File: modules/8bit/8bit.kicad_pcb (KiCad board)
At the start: 2 copper layers, 30.5 x 68.6 mm, 24 parts, among them SW1 MODE SELECT, U1 MCP6002-xSN, U2 ATtiny1616-M, U3 MCP6002-xSN

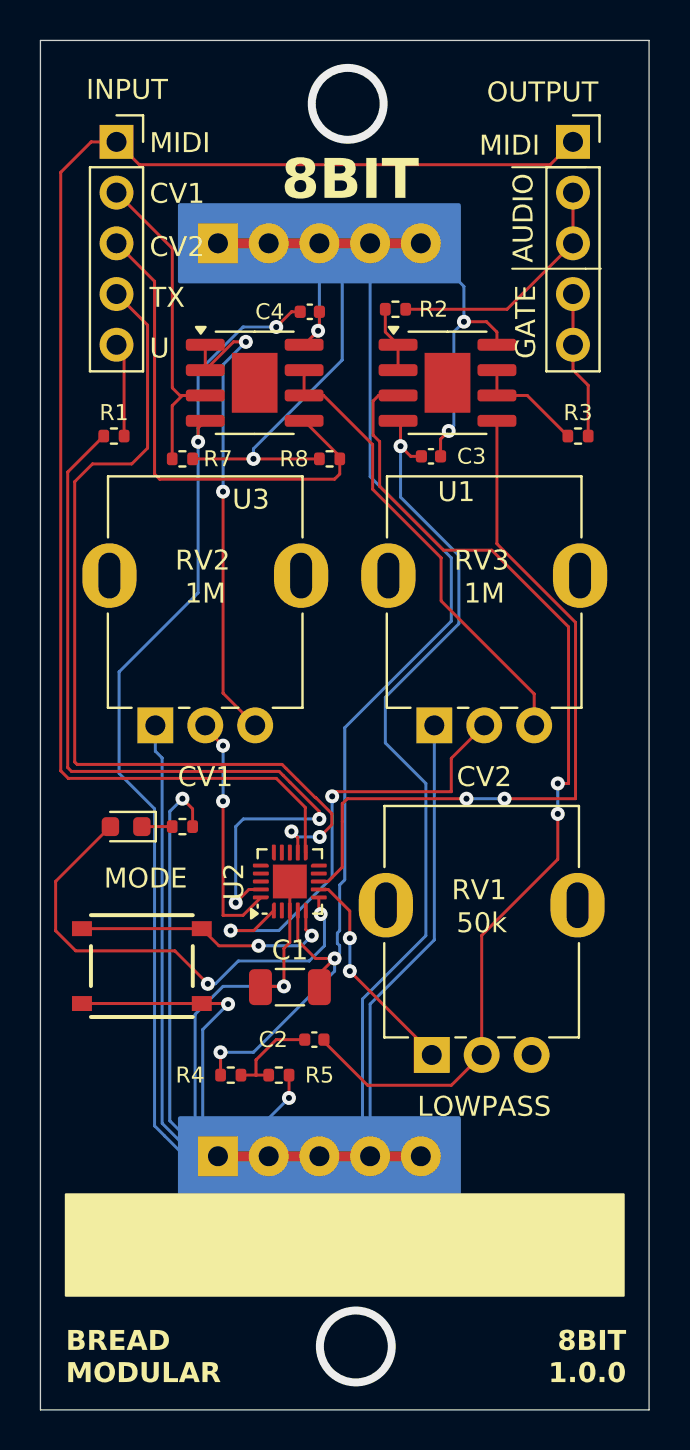
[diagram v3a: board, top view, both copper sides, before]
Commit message: 8bit: Change the push button
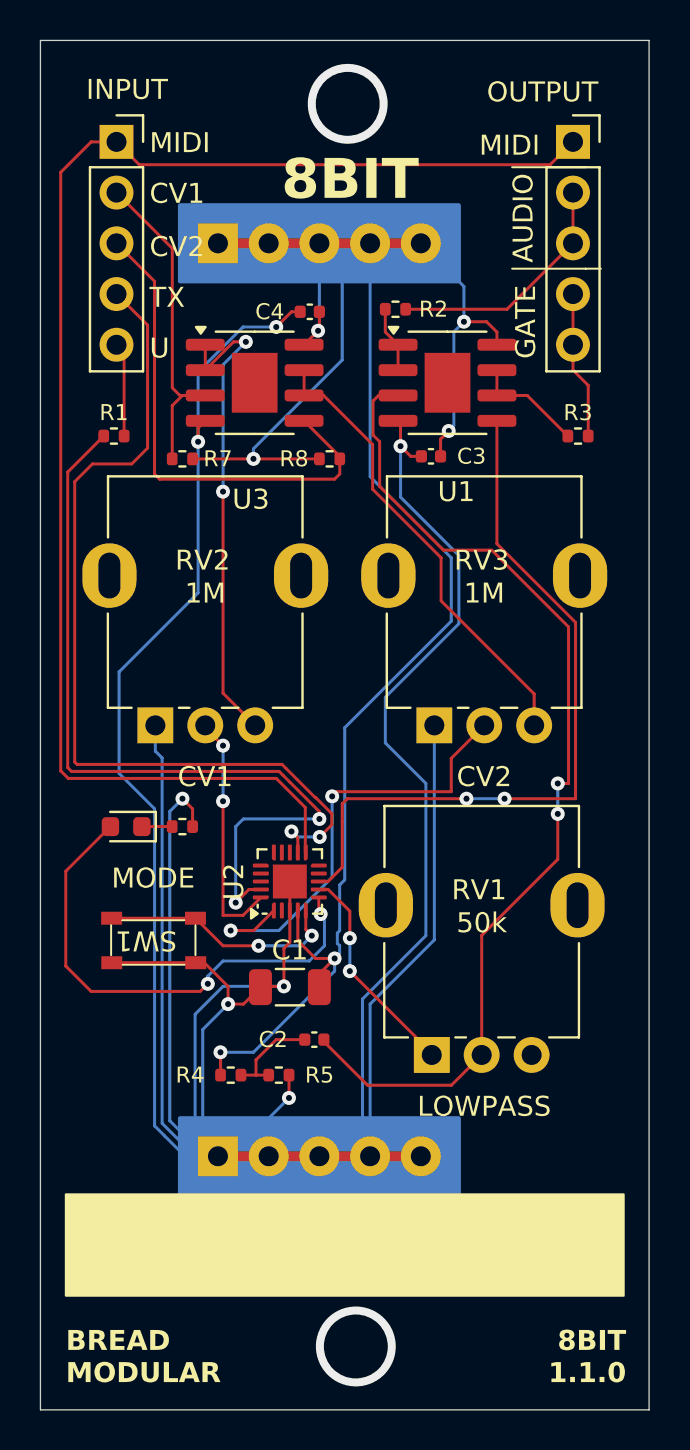
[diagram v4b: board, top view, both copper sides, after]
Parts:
- SW1: footprint BreadModular_MISC:SPST_TS-1187A-B-A-B -> BreadModular_MISC:K2-1808SN-A4SW-01
- moved SW1 1.42 mm to (52.7, 85.7)
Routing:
- net GND: track 211.0 -> 212.8 mm
- net Net-(SW1-B): track 13.5 -> 12.2 mm
- net Net-(D1-A): track 24.2 -> 25.1 mm
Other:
- board text added: "8BIT 1.1.0"
- board text removed: "8BIT 1.0.0"
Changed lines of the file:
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@@
 		)
 	)
-	(footprint "BreadModular_MISC:SPST_TS-1187A-B-A-B"
+	(footprint "BreadModular_MISC:K2-1808SN-A4SW-01"
 		(layer "F.Cu")
-		(at 52.07 86.995 180)
+		(at 52.705 85.725 180)
 		(property "Reference" "SW1"
-			(at 0.032 3.163 0)
-			(layer "F.Fab")
+			(at 0.425 0 180)
+			(unlocked yes)
+			(layer "F.SilkS")
 			(effects
 				(font
-					(size 0.5 0.5)
-					(thickness 0.12)
+					(size 1 1)
+					(thickness 0.1)
 				)
 			)
 		)
 		(property "Value" "MODE SELECT"
-			(at 0 0 0)
+			(at 0.025 2.6 180)
+			(unlocked yes)
 			(layer "F.Fab")
 			(effects
 				(font
-					(size 0.5 0.5)
-					(thickness 0.12)
+					(size 1 1)
+					(thickness 0.15)
 				)
 			)
 		)
-		(property "Footprint" "BreadModular_MISC:SPST_TS-1187A-B-A-B"
-			(at 0 0 0)
+		(property "Footprint" "BreadModular_MISC:K2-1808SN-A4SW-01"
+			(at 2.26 1.125 180)
+			(unlocked yes)
 			(layer "F.Fab")
 			(hide yes)
 			(effects
 				(font
-					(size 1.27 1.27)
+					(size 1 1)
 					(thickness 0.15)
 				)
@@
 		)
 		(property "Datasheet" ""
-			(at 0 0 0)
+			(at 2.26 1.125 180)
+			(unlocked yes)
 			(layer "F.Fab")
 			(hide yes)
 			(effects
 				(font
-					(size 1.27 1.27)
+					(size 1 1)
 					(thickness 0.15)
 				)
@@
 		)
 		(property "Description" "Single Pole Single Throw (SPST) switch"
-			(at 0 0 0)
+			(at 2.26 1.125 180)
+			(unlocked yes)
 			(layer "F.Fab")
 			(hide yes)
 			(effects
 				(font
-					(size 1.27 1.27)
+					(size 1 1)
 					(thickness 0.15)
 				)
@@
 		(sheetname "Root")
 		(sheetfile "8bit.kicad_sch")
-		(attr through_hole)
+		(attr smd)
 		(fp_line
-			(start 2.55 -1)
-			(end 2.55 1)
+			(start 2.175 -0.725)
+			(end 2.175 0.775)
 			(stroke
-				(width 0.2)
-				(type solid)
+				(width 0.1)
+				(type default)
 			)
 			(layer "F.SilkS")
 		)
 		(fp_line
-			(start -2.55 2.55)
-			(end 2.55 2.55)
+			(start -1.49 1.025)
+			(end 1.61 1.025)
 			(stroke
-				(width 0.2)
-				(type solid)
+				(width 0.1)
+				(type default)
 			)
 			(layer "F.SilkS")
 		)
 		(fp_line
-			(start -2.55 -1)
-			(end -2.55 1)
+			(start -1.5 -1.2)
+			(end 1.6 -1.2)
 			(stroke
-				(width 0.2)
-				(type solid)
+				(width 0.1)
+				(type default)
 			)
 			(layer "F.SilkS")
 		)
 		(fp_line
-			(start -2.55 -2.55)
-			(end 2.55 -2.55)
+			(start -2.05 -0.725)
+			(end -2.05 0.775)
 			(stroke
-				(width 0.2)
-				(type solid)
+				(width 0.1)
+				(type default)
 			)
 			(layer "F.SilkS")
 		)
+		(fp_text user "${REFERENCE}"
+			(at 0.025 4.1 180)
+			(unlocked yes)
+			(layer "F.Fab")
+			(effects
+				(font
+					(size 1 1)
+					(thickness 0.15)
+				)
+			)
+		)
 		(pad "1" smd rect
-			(at -3 -1.875 180)
-			(size 1 0.75)
+			(at -2.06 -1.1 180)
+			(size 1.05 0.65)
 			(layers "F.Cu" "F.Paste" "F.Mask")
 			(net 1 "GND")
 			(pinfunction "A")
 			(pintype "passive")
+			(thermal_bridge_angle 45)
 		)
 		(pad "1" smd rect
-			(at 3 -1.875 180)
-			(size 1 0.75)
+			(at 2.14 -1.1 180)
+			(size 1.05 0.65)
 			(layers "F.Cu" "F.Paste" "F.Mask")
 			(net 1 "GND")
 			(pinfunction "A")
 			(pintype "passive")
+			(thermal_bridge_angle 45)
 		)
 		(pad "2" smd rect
-			(at -3 1.875 180)
-			(size 1 0.75)
+			(at -2.05 1.125 180)
+			(size 1.05 0.65)
 			(layers "F.Cu" "F.Paste" "F.Mask")
 			(net 23 "Net-(SW1-B)")
 			(pinfunction "B")
 			(pintype "passive")
+			(thermal_bridge_angle 45)
 		)
 		(pad "2" smd rect
-			(at 3 1.875 180)
-			(size 1 0.75)
+			(at 2.15 1.125 180)
+			(size 1.05 0.65)
 			(layers "F.Cu" "F.Paste" "F.Mask")
 			(net 23 "Net-(SW1-B)")
 			(pinfunction "B")
 			(pintype "passive")
+			(thermal_bridge_angle 45)
 		)
 	)
@@
 	)
 	(gr_text "MODE"
-		(at 50.165 83.185 0)
+		(at 50.546 83.185 0)
 		(layer "F.SilkS")
 		(effects
@@
 		)
 	)
-	(gr_text "8BIT\n1.0.0"
+	(gr_text "8BIT\n1.1.0"
 		(at 76.327 107.95 0)
 		(layer "F.SilkS")
@@
 	)
 	(segment
-		(start 65.532 61.468)
-		(end 65.024 60.96)
+		(start 54.765 86.825)
+		(end 55.196884 86.825)
 		(width 0.15)
 		(layer "F.Cu")
@@
 	)
 	(segment
-		(start 55.07 88.87)
-		(end 56.358 88.87)
-		(width 0.15)
-		(layer "F.Cu")
-		(net 1)
-	)
-	(segment
-		(start 60 54.229)
-		(end 59.563 54.229)
+		(start 57.16 88.9)
+		(end 58.01 88.05)
 		(width 0.15)
 		(layer "F.Cu")
@@
 	)
 	(segment
-		(start 59.44 93.595)
-		(end 59.436 93.599)
+		(start 65.532 61.468)
+		(end 65.024 60.96)
 		(width 0.15)
 		(layer "F.Cu")
@@
 	)
 	(segment
-		(start 49.07 88.87)
-		(end 55.07 88.87)
+		(start 60 54.229)
+		(end 59.563 54.229)
 		(width 0.15)
 		(layer "F.Cu")
@@
 	)
 	(segment
-		(start 56.358 88.87)
-		(end 56.388 88.9)
+		(start 59.44 93.595)
+		(end 59.436 93.599)
 		(width 0.15)
 		(layer "F.Cu")
@@
 	)
 	(segment
+		(start 55.196884 86.825)
+		(end 56.388 88.016116)
+		(width 0.15)
+		(layer "F.Cu")
+		(net 1)
+	)
+	(segment
+		(start 50.565 86.825)
+		(end 54.765 86.825)
+		(width 0.15)
+		(layer "F.Cu")
+		(net 1)
+	)
+	(segment
 		(start 54.8863 60.0487)
 		(end 55.245 59.69)
@@
 	)
 	(segment
+		(start 56.388 88.9)
+		(end 57.16 88.9)
+		(width 0.15)
+		(layer "F.Cu")
+		(net 1)
+	)
+	(segment
 		(start 54.61 79.121)
 		(end 54.61 80.01)
@@
 	)
 	(segment
+		(start 56.388 88.016116)
+		(end 56.388 88.9)
+		(width 0.15)
+		(layer "F.Cu")
+		(net 1)
+	)
+	(segment
 		(start 59.182 88.011)
 		(end 59.182 86.106)
@@
 	)
 	(segment
-		(start 47.752 85.227)
-		(end 47.752 82.753)
+		(start 48.26 86.995)
+		(end 48.26 82.245)
 		(width 0.15)
 		(layer "F.Cu")
@@
 	)
 	(segment
-		(start 60.93 84.298)
-		(end 60.93 83.56)
+		(start 48.26 82.245)
+		(end 50.495 80.01)
 		(width 0.15)
 		(layer "F.Cu")
@@
 	)
 	(segment
-		(start 47.752 82.753)
-		(end 50.495 80.01)
+		(start 49.53 88.265)
+		(end 48.26 86.995)
 		(width 0.15)
 		(layer "F.Cu")
@@
 	)
 	(segment
-		(start 53.721 86.233)
-		(end 48.758 86.233)
+		(start 55.372 87.884)
+		(end 54.991 88.265)
 		(width 0.15)
 		(layer "F.Cu")
@@
 	)
 	(segment
-		(start 48.758 86.233)
-		(end 47.752 85.227)
+		(start 54.991 88.265)
+		(end 49.53 88.265)
 		(width 0.15)
 		(layer "F.Cu")
@@
 	)
 	(segment
-		(start 55.372 87.884)
-		(end 53.721 86.233)
+		(start 60.93 84.298)
+		(end 60.93 83.56)
 		(width 0.15)
 		(layer "F.Cu")
@@
 	)
 	(segment
-		(start 56.896 86.741)
-		(end 55.753 87.884)
+		(start 56.134 86.741)
+		(end 55.372 87.503)
 		(width 0.15)
 		(layer "B.Cu")
@@
 	)
 	(segment
-		(start 61.214 85.979)
-		(end 61.214 84.582)
+		(start 60.452 86.741)
+		(end 56.134 86.741)
 		(width 0.15)
 		(layer "B.Cu")
@@
 	)
 	(segment
-		(start 60.452 86.741)
-		(end 56.896 86.741)
+		(start 55.372 87.503)
+		(end 55.372 87.884)
 		(width 0.15)
 		(layer "B.Cu")
@@
 	)
 	(segment
-		(start 61.214 84.582)
-		(end 61.0235 84.3915)
+		(start 61.0235 84.3915)
+		(end 61.214 84.582)
 		(width 0.15)
 		(layer "B.Cu")
@@
 	)
 	(segment
-		(start 55.753 87.884)
-		(end 55.372 87.884)
+		(start 61.214 84.582)
+		(end 61.214 85.979)
 		(width 0.15)
 		(layer "B.Cu")
@@
 	)
 	(segment
-		(start 55.929 85.979)
-		(end 57.912 85.979)
+		(start 56.134 85.979)
+		(end 54.755 84.6)
 		(width 0.15)
 		(layer "F.Cu")
@@
 	)
 	(segment
-		(start 55.07 85.12)
-		(end 55.929 85.979)
+		(start 57.912 85.979)
+		(end 56.134 85.979)
 		(width 0.15)
 		(layer "F.Cu")
@@
 	)
 	(segment
-		(start 55.07 85.12)
-		(end 49.07 85.12)
+		(start 60.28 85.172)
+		(end 60.579 85.471)
 		(width 0.15)
 		(layer "F.Cu")
@@
 	)
 	(segment
-		(start 60.28 85.172)
-		(end 60.579 85.471)
+		(start 54.755 84.6)
+		(end 50.555 84.6)
 		(width 0.15)
 		(layer "F.Cu")
